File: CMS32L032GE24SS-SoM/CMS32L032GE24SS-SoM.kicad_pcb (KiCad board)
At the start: 2 copper layers, 8 parts, among them U101 CMS32L032GE24SS, U301 AP2127K-ADJ

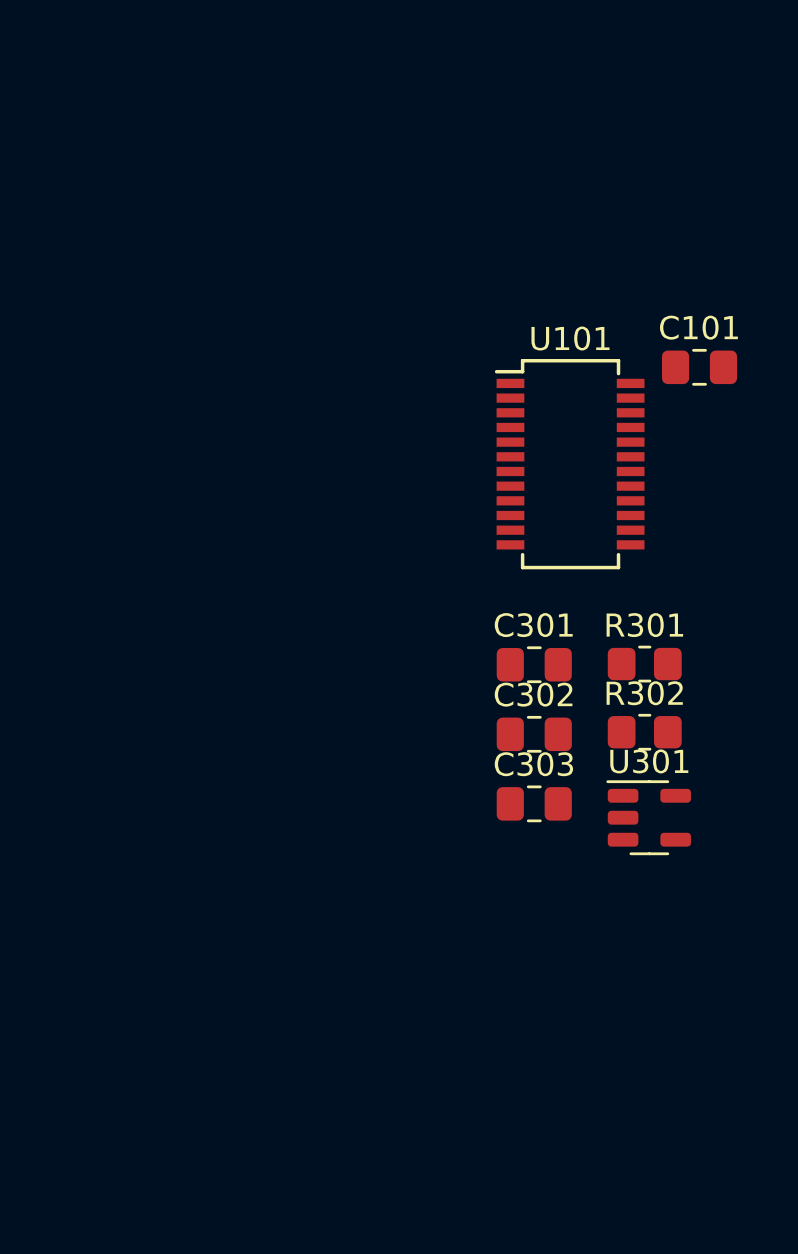
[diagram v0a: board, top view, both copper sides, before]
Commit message: basic layout of chips
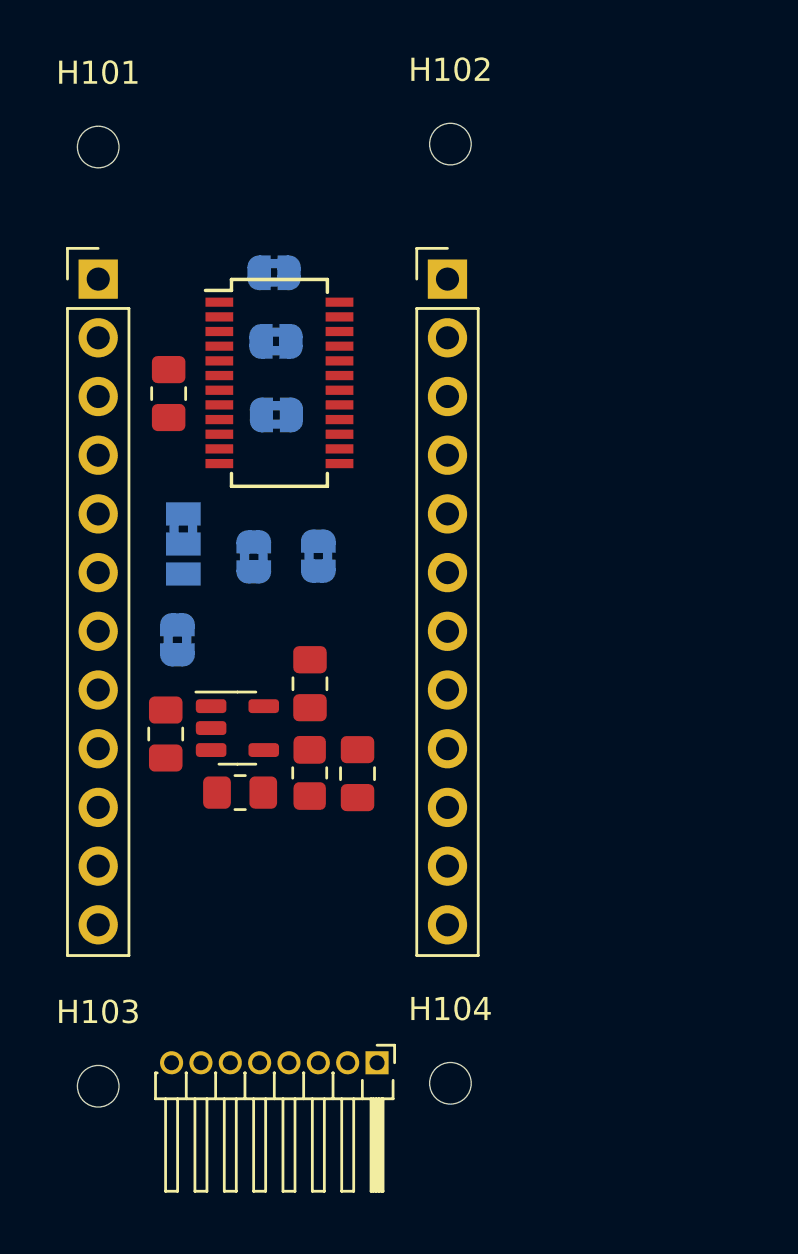
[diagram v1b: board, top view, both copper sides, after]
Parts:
- added H101: MountingHole, IotPi_MountingHoles:MountingHole_1.8mm, F.Cu at (91.7, 50.0)
- added H102: MountingHole, IotPi_MountingHoles:MountingHole_1.8mm, F.Cu at (106.9, 49.9)
- added H103: MountingHole, IotPi_MountingHoles:MountingHole_1.8mm, F.Cu at (91.7, 90.7)
- added H104: MountingHole, IotPi_MountingHoles:MountingHole_1.8mm, F.Cu at (106.9, 90.6)
- added J101: MCU Right Side, Connector_PinHeader_2.54mm:PinHeader_1x12_P2.54mm_Vertical, F.Cu at (106.8, 55.8)
- added J102: MCU Left Side, Connector_PinHeader_2.54mm:PinHeader_1x12_P2.54mm_Vertical, F.Cu at (91.7, 55.8)
- added J105: Connection to DAPLink Board, Connector_PinHeader_1.27mm:PinHeader_1x08_P1.27mm_Horizontal, F.Cu at (103.8, 89.7)
- added JP101: V_{IN} Jumper, Jumper:SolderJumper-3_P1.3mm_Bridged2Bar12_Pad1.0x1.5mm, B.Cu at (95.4, 67.2)
- added JP103: SolderJumper_2_Bridged, Jumper:SolderJumper-2_P1.3mm_Bridged2Bar_RoundedPad1.0x1.5mm, B.Cu at (95.1, 71.4)
- added JP201: SWDCLK Jumper, Jumper:SolderJumper-2_P1.3mm_Bridged2Bar_RoundedPad1.0x1.5mm, B.Cu at (99.4, 58.5)
- added JP202: SWDIO Jumper, Jumper:SolderJumper-2_P1.3mm_Bridged2Bar_RoundedPad1.0x1.5mm, B.Cu at (99.4, 61.6)
- added JP203: MCU_VDD Jumper, Jumper:SolderJumper-2_P1.3mm_Bridged2Bar_RoundedPad1.0x1.5mm, B.Cu at (99.3, 55.5)
- added JP204: MCU UART TX Jumper, Jumper:SolderJumper-2_P1.3mm_Bridged2Bar_RoundedPad1.0x1.5mm, B.Cu at (98.4, 67.8)
- added JP205: MCU UART RX Jumper, Jumper:SolderJumper-2_P1.3mm_Bridged2Bar_RoundedPad1.0x1.5mm, B.Cu at (101.2, 67.7)
- moved C101 23.0 mm to (94.7, 60.7), turned to 90 degrees
- moved U301 18.2 mm to (97.7, 75.2)
- moved R302 17.7 mm to (97.8, 78.0), turned to 180 degrees
- moved C301 16.2 mm to (94.6, 75.4), turned to -90 degrees
- moved R301 15.2 mm to (100.8, 77.1), turned to 90 degrees
- moved U101 13.1 mm to (99.5, 60.2)
- moved C302 9.95 mm to (100.9, 73.3), turned to 90 degrees
- moved C303 7.76 mm to (102.9, 77.2), turned to -90 degrees
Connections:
- net /V_{IN} renamed /Regulator_V_{IN}
- C101 pad 1: /CMS32L032GE24SS/V_{IN} -> /MCU_V_{IN}
- C302 pad 1: /CMS32L032GE24SS/V_{IN} -> /Regulator_V_{OUT}
- C303 pad 1: /CMS32L032GE24SS/V_{IN} -> /Regulator_V_{OUT}
- R301 pad 2: /CMS32L032GE24SS/V_{IN} -> /Regulator_V_{OUT}
- U101 pad 9: /CMS32L032GE24SS/V_{IN} -> /MCU_V_{IN}
- U301 pad 5: /CMS32L032GE24SS/V_{IN} -> /Regulator_V_{OUT}

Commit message: locked ArduinoNano board
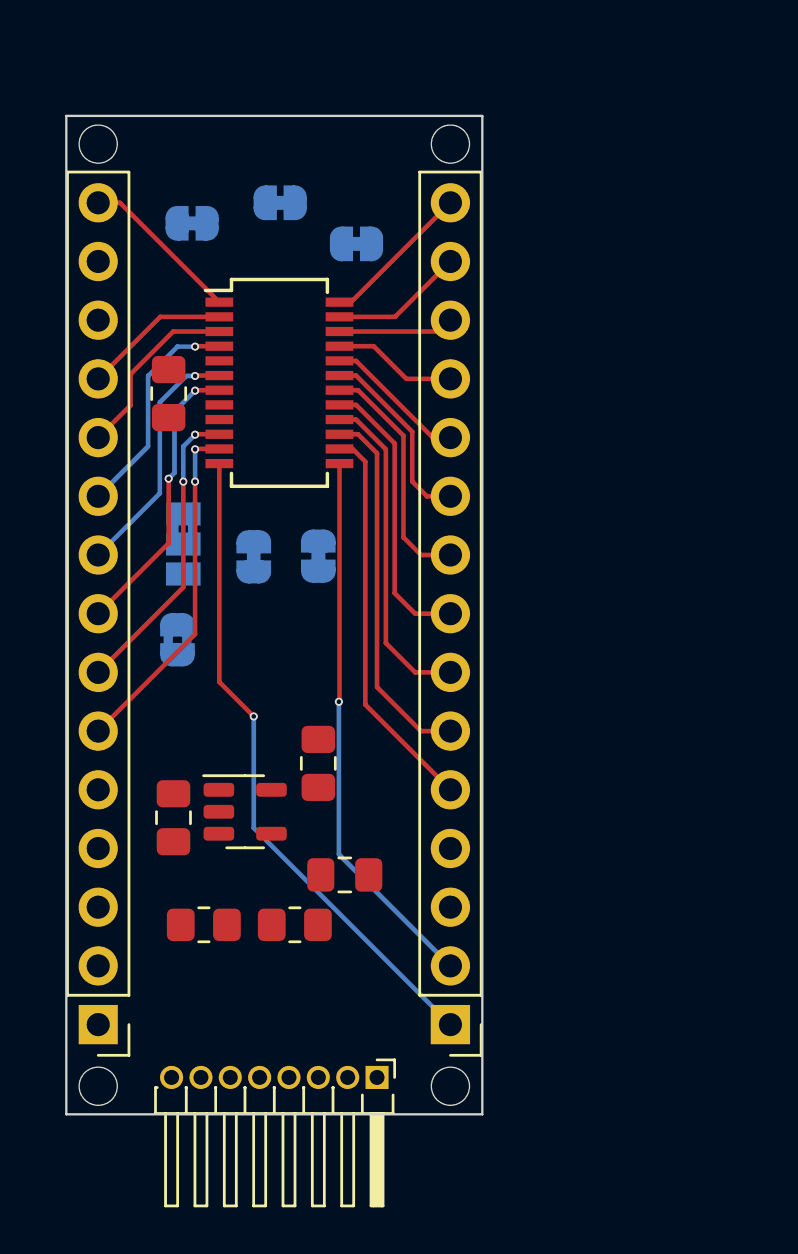
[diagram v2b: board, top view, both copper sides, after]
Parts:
- J101, J102: footprint Connector_PinHeader_2.54mm:PinHeader_1x12_P2.54mm_Vertical -> Connector_PinHeader_2.54mm:PinHeader_1x15_P2.54mm_Vertical
- JP201, JP202, JP203, JP204, JP205: footprint Jumper:SolderJumper-2_P1.3mm_Bridged2Bar_RoundedPad1.0x1.5mm -> Jumper:SolderJumper-2_P1.3mm_Bridged_RoundedPad1.0x1.5mm
- moved J101 32.3 mm to (106.9, 88.0), turned to 180 degrees
- moved J102 32.3 mm to (91.7, 88.0), turned to 180 degrees
- moved JP202 9.06 mm to (95.8, 53.3)
- moved R301 6.60 mm to (100.2, 83.7), turned to 0 degrees
- moved R302 5.93 mm to (96.3, 83.7)
- moved JP201 5.47 mm to (102.9, 54.2)
- moved C303 4.42 mm to (102.4, 81.5), turned to 0 degrees
- moved U301 3.64 mm to (98.1, 78.8)
- moved C301 3.64 mm to (95.0, 79.1)
- moved C302 3.47 mm to (101.2, 76.7)
- moved JP203 3.04 mm to (99.6, 52.5)
- moved J105 0.63 mm to (103.8, 90.3)
- moved H101 0.13 mm to (91.7, 49.9)
- moved H104 0.13 mm to (106.9, 90.7)
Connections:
- C101 pad 1: /MCU_V_{IN} -> /V_{IN}
- J101 pad 1: /CMS32L032GE24SS/MCU_PIN_1 -> /CMS32L032GE24SS/MCU_PIN_12_UART_TX
- J101 pad 10: /CMS32L032GE24SS/MCU_PIN_10 -> /CMS32L032GE24SS/MCU_PIN_19
- J101 pad 11: /CMS32L032GE24SS/MCU_PIN_11 -> /CMS32L032GE24SS/MCU_PIN_20
- J101 pad 12: /CMS32L032GE24SS/MCU_PIN_12 -> /CMS32L032GE24SS/MCU_PIN_21
- J101 pad 2: /CMS32L032GE24SS/MCU_PIN_2 -> /CMS32L032GE24SS/MCU_PIN_13_UART_RX
- J101 pad 3: /CMS32L032GE24SS/MCU_PIN_3 -> /CMS32L032GE24SS/MCU_PIN_RESET
- J101 pad 4: /CMS32L032GE24SS/MCU_PIN_4 -> GND
- J101 pad 5: /CMS32L032GE24SS/MCU_PIN_5 -> /CMS32L032GE24SS/MCU_PIN_14
- J101 pad 6: /CMS32L032GE24SS/MCU_PIN_6 -> /CMS32L032GE24SS/MCU_PIN_15
- J101 pad 7: /CMS32L032GE24SS/MCU_PIN_7 -> /CMS32L032GE24SS/MCU_PIN_16
- J101 pad 8: /MCU_V_{IN} -> /CMS32L032GE24SS/MCU_PIN_17
- J101 pad 9: GND -> /CMS32L032GE24SS/MCU_PIN_18
- J102 pad 1: /CMS32L032GE24SS/MCU_PIN_24 -> /V_{IN}
- J102 pad 10: /CMS32L032GE24SS/MCU_PIN_15 -> /CMS32L032GE24SS/MCU_PIN_4
- J102 pad 11: /CMS32L032GE24SS/MCU_PIN_14 -> /CMS32L032GE24SS/MCU_PIN_3
- J102 pad 12: /CMS32L032GE24SS/MCU_PIN_13 -> /CMS32L032GE24SS/MCU_PIN_2
- J102 pad 2: /CMS32L032GE24SS/MCU_PIN_23 -> GND
- J102 pad 3: /CMS32L032GE24SS/MCU_PIN_22 -> /CMS32L032GE24SS/MCU_PIN_RESET
- J102 pad 4: /CMS32L032GE24SS/MCU_PIN_21 -> /V_{IN}
- J102 pad 5: /CMS32L032GE24SS/MCU_PIN_20 -> unconnected-(J102-Pin_5-Pad5)
- J102 pad 6: /CMS32L032GE24SS/MCU_PIN_19 -> /CMS32L032GE24SS/MCU_PIN_11
- J102 pad 7: /CMS32L032GE24SS/MCU_PIN_18 -> /CMS32L032GE24SS/MCU_PIN_10
- J102 pad 8: /CMS32L032GE24SS/MCU_PIN_17 -> /CMS32L032GE24SS/MCU_PIN_7
- J102 pad 9: /CMS32L032GE24SS/MCU_PIN_16 -> /CMS32L032GE24SS/MCU_PIN_6
- JP203 pad 1: /MCU_V_{IN} -> /V_{IN}
- JP204 pad 1: /CMS32L032GE24SS/MCU_PIN_12 -> /CMS32L032GE24SS/MCU_PIN_12_UART_TX
- JP205 pad 1: /CMS32L032GE24SS/MCU_PIN_13 -> /CMS32L032GE24SS/MCU_PIN_13_UART_RX
- U101 pad 12: /CMS32L032GE24SS/MCU_PIN_12 -> /CMS32L032GE24SS/MCU_PIN_12_UART_TX
- U101 pad 13: /CMS32L032GE24SS/MCU_PIN_13 -> /CMS32L032GE24SS/MCU_PIN_13_UART_RX
- U101 pad 5: /CMS32L032GE24SS/MCU_PIN_5 -> /CMS32L032GE24SS/MCU_PIN_RESET
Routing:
- net /CMS32L032GE24SS/MCU_PIN_12_UART_TX: track 0.00 -> 28.4 mm, vias 0 -> 1
- net /CMS32L032GE24SS/MCU_PIN_13_UART_RX: track 0.00 -> 23.7 mm, vias 0 -> 1
- net /CMS32L032GE24SS/MCU_PIN_14: track 0.00 -> 17.1 mm
- net /CMS32L032GE24SS/MCU_PIN_15: track 0.00 -> 16.0 mm
- net /CMS32L032GE24SS/MCU_PIN_11: track 0.00 -> 15.0 mm, vias 0 -> 2
- net /CMS32L032GE24SS/MCU_PIN_16: track 0.00 -> 14.2 mm
- net /CMS32L032GE24SS/MCU_PIN_10: track 0.00 -> 13.1 mm, vias 0 -> 2
- net /CMS32L032GE24SS/MCU_PIN_7: track 0.00 -> 12.4 mm, vias 0 -> 2
- net /CMS32L032GE24SS/MCU_PIN_17: track 0.00 -> 12.3 mm
- net /CMS32L032GE24SS/MCU_PIN_6: track 0.00 -> 10.8 mm, vias 0 -> 1
- net /CMS32L032GE24SS/MCU_PIN_18: track 0.00 -> 10.3 mm
- net /CMS32L032GE24SS/MCU_PIN_4: track 0.00 -> 9.72 mm, vias 0 -> 1
- net /CMS32L032GE24SS/MCU_PIN_19: track 0.00 -> 8.23 mm
- net /CMS32L032GE24SS/MCU_PIN_3: track 0.00 -> 7.93 mm
- net /CMS32L032GE24SS/MCU_PIN_1: track 0.00 -> 7.02 mm
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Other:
- board outline added: 18 x 43.2 mm

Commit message: routing
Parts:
- H101, H102, H103, H104: footprint IotPi_MountingHoles:MountingHole_1.8mm -> IotPi_ArduinoNanoMountingHoles:ArduinoNano_MountingHole
- J105: footprint Connector_PinHeader_1.27mm:PinHeader_1x08_P1.27mm_Horizontal -> Connector_PinHeader_1.27mm:PinHeader_1x08_P1.27mm_Vertical
- JP101: moved to F.Cu
- moved JP201 33.5 mm to (96.1, 87.0), turned to -90 degrees
- moved JP202 33.4 mm to (103.4, 85.9), turned to -90 degrees
- moved JP103 7.26 mm to (94.9, 78.6), turned to 90 degrees
- moved JP101 6.18 mm to (98.9, 72.3), turned to 180 degrees
- moved C302 1.53 mm to (102.2, 77.9), turned to 0 degrees
- moved JP203 1.40 mm to (99.4, 53.8)
- moved JP204 1.10 mm to (98.4, 66.7)
- moved JP205 1.07 mm to (101.1, 66.7)
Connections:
- C101 pad 1: /V_{IN} -> /MCU_V_{IN}
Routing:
- net /CMS32L032GE24SS/MCU_PIN_RESET: track 0.00 -> 56.4 mm, vias 0 -> 3
- net /V_{IN}: track 0.00 -> 42.8 mm, vias 0 -> 2
- net /MCU_V_{IN}: track 0.00 -> 26.8 mm, vias 0 -> 2
- net /UART_TX: track 0.00 -> 24.6 mm
- net /UART_RX: track 0.00 -> 24.5 mm, vias 0 -> 1
- net /Regulator_V_{IN}: track 0.00 -> 10.8 mm, vias 0 -> 2
- net /Regulator_V_{OUT}: track 0.00 -> 6.19 mm
- net /CMS32L032GE24SS/MCU_PIN_12_UART_TX: track 28.4 -> 34.2 mm, vias 1 -> 2
- net Net-(U301-ADJ): track 0.00 -> 1.94 mm
- net /CMS32L032GE24SS/MCU_PIN_13_UART_RX: track 23.7 -> 25.6 mm, vias 1 -> 2
- added copper zone on F.Cu, net /Regulator_V_{OUT}
- added copper zone on B.Cu, net /V_{IN}
- added copper zone on B.Cu, net GND
- added copper zone on F.Cu, net GND

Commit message: finished layout and routing
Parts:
- removed JP103: SolderJumper_2_Bridged, Jumper:SolderJumper-2_P1.3mm_Bridged2Bar_RoundedPad1.0x1.5mm
- removed JP203: MCU_VDD Jumper, Jumper:SolderJumper-2_P1.3mm_Bridged_RoundedPad1.0x1.5mm
- J101, J102, JP101: moved to B.Cu
- moved JP201 28.2 mm to (97.4, 58.8)
- moved JP202 27.3 mm to (100.1, 58.8)
- moved JP204 1.27 mm to (97.7, 67.7)
- moved JP205 1.27 mm to (100.3, 67.7)
- turned J101 to 0 degrees
- turned J102 to 0 degrees
- turned JP101 to 0 degrees
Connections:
- C301 pad 1: /Regulator_V_{IN} -> /V_{IN}
- J102 pad 14: /MCU_V_{IN} -> /Regulator_V_{OUT}
- J102 pad 4: /V_{IN} -> /MCU_V_{IN}
- J102 pad 5: unconnected-(J102-Pin_5-Pad5) -> /CMS32L032GE24SS/MCU_PIN_12_UART_TX
- J105 pad 1: /V_{IN} -> /UART_TX
- J105 pad 2: /MCU_SWDCLK -> /UART_RX
- J105 pad 3: /MCU_SWDIO -> /MCU_SWDCLK
- J105 pad 4: /MCU_SWO -> /MCU_SWDIO
- J105 pad 5: /UART_TX -> /MCU_SWO
- J105 pad 6: /UART_RX -> /MCU_V_{IN}
- J105 pad 7: /MCU_VDD -> /V_{IN}
- JP101 pad 1: /Regulator_V_{OUT} -> /V_{IN}
- JP101 pad 3: /V_{IN} -> /Regulator_V_{OUT}
- U301 pad 1: /Regulator_V_{IN} -> /V_{IN}
- U301 pad 3: /Regulator_V_{IN} -> /V_{IN}
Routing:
- net /Regulator_V_{OUT}: track 6.19 -> 51.9 mm, vias 0 -> 6
- net /MCU_SWDCLK: track 0.00 -> 32.4 mm, vias 0 -> 2
- net /MCU_SWDIO: track 0.00 -> 32.0 mm, vias 0 -> 3
- net /MCU_V_{IN}: track 26.8 -> 39.0 mm
- net /CMS32L032GE24SS/MCU_PIN_RESET: track 56.4 -> 44.8 mm
- net /Regulator_V_{IN}: track 10.8 -> 0.00 mm, vias 2 -> 0
- net /V_{IN}: track 42.8 -> 33.2 mm, vias 2 -> 3
- net /CMS32L032GE24SS/MCU_PIN_23: track 5.79 -> 10.8 mm, vias 0 -> 1
- net /CMS32L032GE24SS/MCU_PIN_12_UART_TX: track 34.2 -> 38.9 mm, vias 2 -> 4
- net Net-(U301-ADJ): track 1.94 -> 5.88 mm
- net /CMS32L032GE24SS/MCU_PIN_22: track 5.00 -> 7.11 mm, vias 0 -> 1
- net /UART_RX: track 24.5 -> 22.9 mm
- net /CMS32L032GE24SS/MCU_PIN_13_UART_RX: track 25.6 -> 27.0 mm
- net /UART_TX: track 24.6 -> 25.8 mm, vias 0 -> 1
- net /CMS32L032GE24SS/MCU_PIN_15: track 16.0 -> 15.3 mm
- added copper zone on B.Cu, net /Regulator_V_{OUT}
- added copper zone on F.Cu, net /V_{IN}
